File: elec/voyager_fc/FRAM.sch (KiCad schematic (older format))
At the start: 3 parts

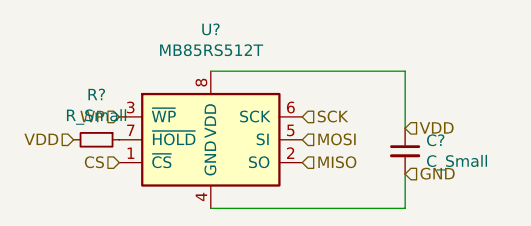
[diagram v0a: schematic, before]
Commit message: Place all components and start route
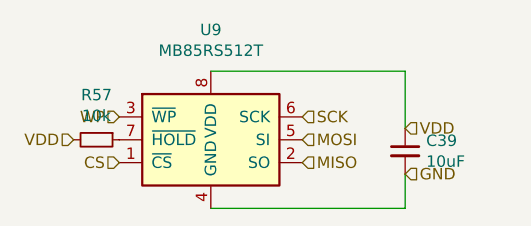
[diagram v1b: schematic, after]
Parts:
- C39: renamed from C?; value C_Small -> 10uF; footprint (none) -> Capacitor_SMD:C_0603_1608Metric
- R57: renamed from R?; value R_Small -> 10k; footprint (none) -> Resistor_SMD:R_0603_1608Metric
- U9: renamed from U?; footprint (none) -> MB85RS512TPNF-G-JNERE1:SOIC127P600X88-8N
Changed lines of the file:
@@
 $Descr A4 11693 8268
 encoding utf-8
-Sheet 9 9
+Sheet 8 10
 Title ""
 Date ""
@@
 P 5750 4150
 AR Path="/679818F2" Ref="U?"  Part="1"
-AR Path="/67980E8D/679818F2" Ref="U?"  Part="1"
-F 0 "U?" H 5750 4631 50  0000 C CNN
+AR Path="/67980E8D/679818F2" Ref="U9"  Part="1"
+F 0 "U9" H 5750 4631 50  0000 C CNN
 F 1 "MB85RS512T" H 5750 4540 50  0000 C CNN
-F 2 "" H 5400 4100 50  0001 C CNN
+F 2 "MB85RS512TPNF-G-JNERE1:SOIC127P600X88-8N" H 5400 4100 50  0001 C CNN
 F 3 "http://www.fujitsu.com/downloads/MICRO/fsa/pdf/products/memory/fram/MB85RS16-DS501-00014-6v0-E.pdf" H 5400 4100 50  0001 C CNN
 	1    5750 4150
@@
 VDD
 $Comp
-L Device:R_Small R?
+L Device:R_Small R57
 U 1 1 6798CA35
 P 5250 4150
-F 0 "R?" V 5054 4150 50  0000 C CNN
-F 1 "R_Small" V 5145 4150 50  0000 C CNN
-F 2 "" H 5250 4150 50  0001 C CNN
+F 0 "R57" V 5054 4150 50  0000 C CNN
+F 1 "10k" V 5145 4150 50  0000 C CNN
+F 2 "Resistor_SMD:R_0603_1608Metric" H 5250 4150 50  0001 C CNN
 F 3 "~" H 5250 4150 50  0001 C CNN
 	1    5250 4150
@@
 WP
 $Comp
-L Device:C_Small C?
+L Device:C_Small C39
 U 1 1 6798DE5C
 P 6600 4200
-F 0 "C?" H 6692 4246 50  0000 L CNN
-F 1 "C_Small" H 6692 4155 50  0000 L CNN
-F 2 "" H 6600 4200 50  0001 C CNN
+F 0 "C39" H 6692 4246 50  0000 L CNN
+F 1 "10uF" H 6692 4155 50  0000 L CNN
+F 2 "Capacitor_SMD:C_0603_1608Metric" H 6600 4200 50  0001 C CNN
 F 3 "~" H 6600 4200 50  0001 C CNN
 	1    6600 4200
